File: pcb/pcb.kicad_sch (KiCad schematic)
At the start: 61 parts, among them CN1 Pump_Drain, CN10 VIMM, CN11 VBUS, CN2 Soil_Drain, CN3 ~{Soil_On}, CN4 Soil_Out, CN5 Pump_On, CN6 Water_Out, CN7 3.3V, CN8 Bat_Sense, CN9 Battery, Q2 2N7002, Q4 AO3400A, Q5 AO3401A, U1 TPS63802DLAT, U2 ESP-32S DevBoard, U3 BQ24075RGTR, U5 HX TYPE-C 6PIN, U6 TUSB320LIRWBR, U7 Pump, U8 Water_Sensor

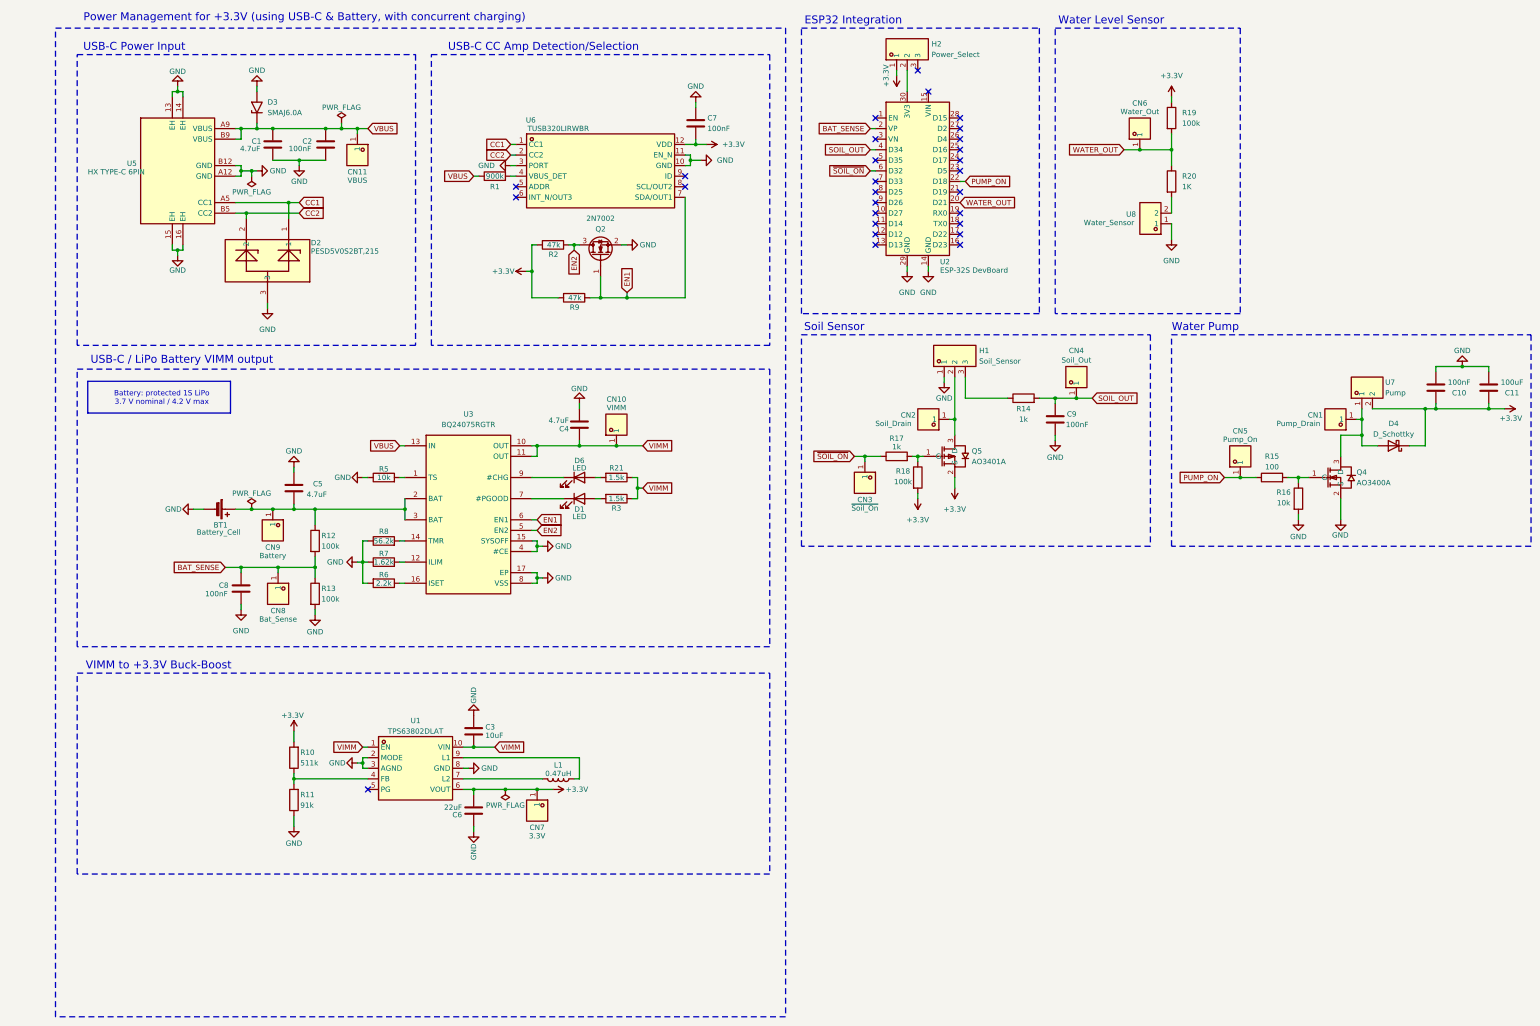
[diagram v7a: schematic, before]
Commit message: Replaced all the resistors with 0805 LCSC components
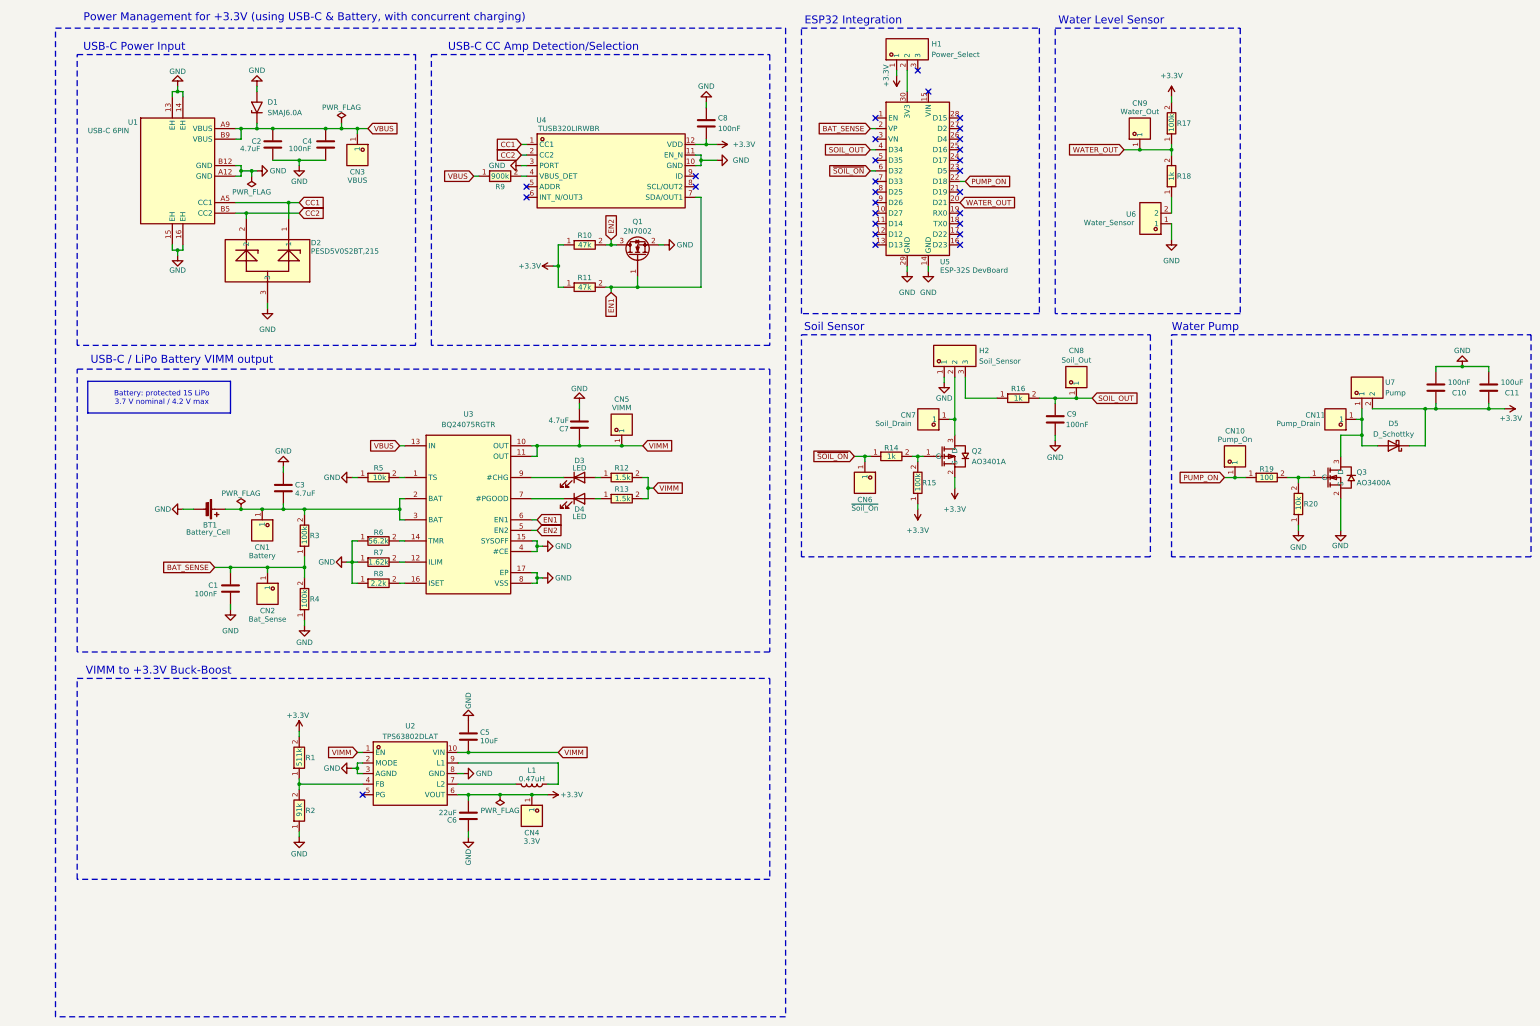
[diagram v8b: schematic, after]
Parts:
- removed R1: 900k, Resistor_SMD:R_1206_3216Metric_Pad1.30x1.75mm_HandSolder, symbol Device:R
- removed R10: 511k, Resistor_SMD:R_1206_3216Metric_Pad1.30x1.75mm_HandSolder, symbol Device:R
- removed R11: 91k, Resistor_SMD:R_1206_3216Metric_Pad1.30x1.75mm_HandSolder, symbol Device:R
- removed R12, R13, R18, R19: 100k, Resistor_SMD:R_1206_3216Metric_Pad1.30x1.75mm_HandSolder, symbol Device:R
- removed R14, R17: 1k, Resistor_SMD:R_1206_3216Metric_Pad1.30x1.75mm_HandSolder, symbol Device:R
- removed R15: 100, Resistor_SMD:R_1206_3216Metric_Pad1.30x1.75mm_HandSolder, symbol Device:R
- removed R16, R5: 10k, Resistor_SMD:R_1206_3216Metric_Pad1.30x1.75mm_HandSolder, symbol Device:R
- removed R2, R9: 47k, Resistor_SMD:R_1206_3216Metric_Pad1.30x1.75mm_HandSolder, symbol Device:R
- removed R20: 1K, Resistor_SMD:R_1206_3216Metric_Pad1.30x1.75mm_HandSolder, symbol Device:R
- removed R21, R3: 1.5k, Resistor_SMD:R_1206_3216Metric_Pad1.30x1.75mm_HandSolder, symbol Device:R
- removed R6: 2.2k, Resistor_SMD:R_1206_3216Metric_Pad1.30x1.75mm_HandSolder, symbol Device:R
- removed R7: 1.62k, Resistor_SMD:R_1206_3216Metric_Pad1.30x1.75mm_HandSolder, symbol Device:R
- removed R8: 56.2k, Resistor_SMD:R_1206_3216Metric_Pad1.30x1.75mm_HandSolder, symbol Device:R
- added R1: 511k, EasyEDA:R0805, symbol EasyEDA:0805R 511k
- added R10, R11: 47k, EasyEDA:R0805, symbol EasyEDA:0805R 47k
- added R12, R13: 1.5k, EasyEDA:R0805, symbol EasyEDA:0805R 1.5k
- added R14, R16, R18: 1k, EasyEDA:R0805, symbol EasyEDA:0805R 1k
- added R15, R17, R3, R4: 100k, EasyEDA:R0805, symbol EasyEDA:0805R 100k
- added R19: 100, EasyEDA:R0805, symbol EasyEDA:0805R 100
- added R2: 91k, EasyEDA:R0805, symbol EasyEDA:0805R 91k
- added R20, R5: 10k, EasyEDA:R0805, symbol EasyEDA:0805R 10k
- added R6: 56.2k, EasyEDA:R0805, symbol EasyEDA:0805R 56.2k
- added R7: 1.62k, EasyEDA:R0805, symbol EasyEDA:0805R 1.62k
- added R8: 2.2k, EasyEDA:R0805, symbol EasyEDA:0805R 2.2k
- added R9: 900k, EasyEDA:R0805, symbol EasyEDA:0805R 900k
- U1: renamed from U5; value HX TYPE-C 6PIN -> USB-C 6PIN
- renumbered C8 to C1, C1 to C2, C5 to C3, C2 to C4, C3 to C5, C4 to C7, C7 to C8, CN9 to CN1, CN5 to CN10, CN1 to CN11, CN8 to CN2, CN11 to CN3, CN7 to CN4, CN10 to CN5, CN3 to CN6, CN2 to CN7, CN4 to CN8, CN6 to CN9, D3 to D1, D6 to D3, D1 to D4, D4 to D5, H2 to H1, H1 to H2, Q2 to Q1, Q5 to Q2, Q4 to Q3, U1 to U2, U6 to U4, U2 to U5, U8 to U6
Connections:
- net +3.3V: now also R1.2, R10.1, R11.1, R15.1, R17.2
- net BAT_SENSE: now also R3.1, R4.2
- net EN1: now also R11.2
- net EN2: now also R10.2
- net GND: now also R2.1, R20.1, R4.1, R5.1, R6.1, R7.1, R8.1
- net PUMP_ON: now also R19.1
- net SOIL_OUT: now also R16.2
- net VBUS: now also R9.1
- net VIMM: now also R12.2, R13.2
- net WATER_OUT: now also R17.1, R18.2
- net ~{SOIL_ON}: now also R14.1
- net at D4.2 (A): now also R13.1
- net at U2.4 (FB): now also R1.1, R2.2
- net at Q3.1 (G): now also R19.2, R20.2
- net at U4.4 (VBUS_DET): now also R9.2
- net at U6.2: now also R18.1
- net at BT1.1 (+), C3.1, CN1.1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: now also R3.2
- net at U3.14 (TMR): now also R6.2
- net at U3.16 (ISET): now also R8.2
- net at Q2.1 (G): now also R14.2, R15.2
- net at H2.3: now also R16.1
- net at U3.1 (TS): now also R5.2
- net at U3.12 (ILIM): now also R7.2
- net at D3.2 (A): now also R12.1
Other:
- moved on the sheet: BT1, C1, C3, C5, C6, C8, CN1, CN10, CN2, CN4, CN5, L1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
